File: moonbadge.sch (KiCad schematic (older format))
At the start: 49 parts, among them J1 Conn_02x03_Top_Bottom, Q2 Q_NMOS_GSD, T1 TEST_1P, T2 TEST_1P, T3 TEST_1P, T4 TEST_1P, T5 TEST_1P, T6 TEST_1P, U1 ESP32-WROOM, U2 XC9141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

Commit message: board done.
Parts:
- removed 3V3, BAT1, EN1, GND1, IO0, RXD1, TXD1: TestPoint, test_point:test_point, symbol Connector:TestPoint
- removed C15: 220uF, Capacitors_SMD:CP_Elec_6.3x5.7, symbol oshw2018badgeprototype-rescue:CP
- removed J1: Conn_02x03_Top_Bottom, Socket_Strips:Socket_Strip_Straight_2x03_Pitch2.54mm, symbol oshw2018badgeprototype-rescue:Conn_02x03_Top_Bottom
- added C15, C17, C3: 10uF, Capacitor_SMD:C_0603_1608Metric, symbol oshw2018badgeprototype-rescue:C
- added C18, C20: 1uF, Capacitor_SMD:C_0603_1608Metric, symbol oshw2018badgeprototype-rescue:C
- added D4, D5: D_Schottky, Diode_SMD:D_SOD-123, symbol oshw2018badgeprototype-rescue:D_Schottky
- added J1, J6: Conn_01x04, Connector_PinHeader_1.27mm:PinHeader_1x04_P1.27mm_Vertical, symbol Connector_Generic:Conn_01x04
- added J10: 105162-0001, 105162-0001:105162-0001, symbol oshw2018badgeprototype-rescue:105162-0001
- added J2: USB_B_Micro, Connector_USB:USB_Micro-B_Molex_47346-0001, symbol Connector:USB_B_Micro
- added J3, J4, J5, J7, J8, J9: Conn_01x02, Connector_PinHeader_1.27mm:PinHeader_1x02_P1.27mm_Vertical, symbol Connector_Generic:Conn_01x02
- added Q1, Q3: PN2222A, Package_TO_SOT_SMD:SOT-23, symbol Transistor_BJT:PN2222A
- added R11, R8: 1k, Capacitor_SMD:C_0603_1608Metric, symbol oshw2018badgeprototype-rescue:R
- added R5, R6: 10K, Capacitor_SMD:C_0603_1608Metric, symbol oshw2018badgeprototype-rescue:R
- added R7: 100k, Capacitor_SMD:C_0603_1608Metric, symbol oshw2018badgeprototype-rescue:R
- added U4: AP1117-33, Package_TO_SOT_SMD:SOT-223-3_TabPin2, symbol Regulator_Linear:AP1117-33
- added U5: CH340G, Package_SO:SOIC-16_3.9x9.9mm_P1.27mm, symbol Interface_USB:CH340G
- BT1: footprint Measurement_Points:Test_Point_Keystone_5019_Minature -> 12BH321P-GR:12BH321P-GR
- C1, C10, C11, C12, C13, C14, C16, C2, C4, C5, C6, C7, C8, C9: footprint Capacitors_SMD:C_0603 -> Capacitor_SMD:C_0603_1608Metric
- C19: footprint Capacitors_SMD:CP_Elec_6.3x5.7 -> Capacitor_SMD:CP_Elec_6.3x5.7
- D1, D2, D3: footprint Diodes_SMD:D_SOD-123 -> Diode_SMD:D_SOD-123
- L1, L2: footprint Inductors_SMD:L_1812 -> Inductor_SMD:L_1812_4532Metric
- Q2: footprint TO_SOT_Packages_SMD:SOT-23 -> Package_TO_SOT_SMD:SOT-23
- R1, R10, R12, R13, R2, R3, R4, R9: footprint Resistors_SMD:R_0603 -> Capacitor_SMD:C_0603_1608Metric
- T1, T2, T3, T4, T5, T6: footprint SMD_Packages:1Pin -> TestPoint:TestPoint_Pad_D2.5mm
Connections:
- net labels added: +5V, DTR, RTS
- wire segments 184 -> 230
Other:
- note removed: "Closing SW asserts EN powing system.\nESP then pulls DCDCEN high to keep system "on"\nESP can shut itself off by setting DCDCEN low."

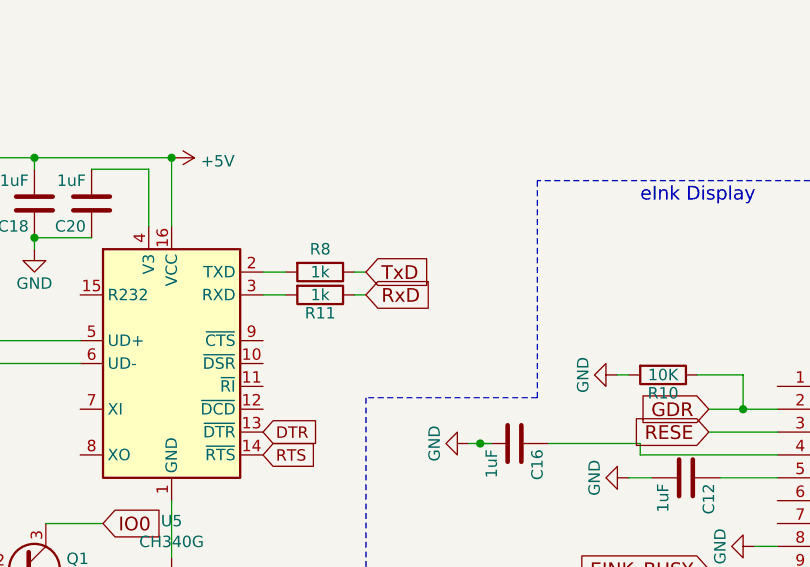
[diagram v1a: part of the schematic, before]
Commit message: Rev 2
Swapped TX/RX
Swapped battery polarity
nudged battery down by 1mm to clear boost coil
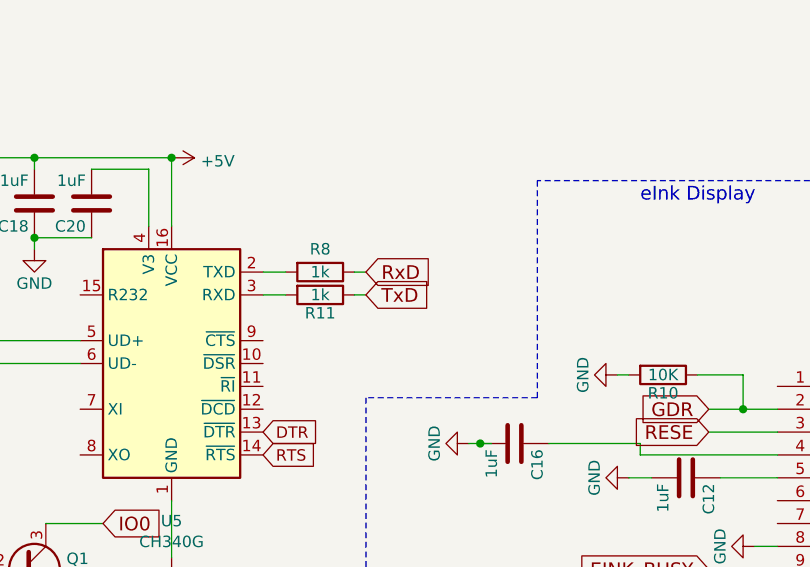
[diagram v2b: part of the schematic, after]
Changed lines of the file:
@@
 Wire Wire Line
 	6950 2050 6950 2300
+Text GLabel 7800 1150 2    60   Input ~ 0
+TxD
 Text GLabel 7800 1050 2    60   Input ~ 0
-TxD
-Text GLabel 7800 1150 2    60   Input ~ 0
 RxD
 $Comp
